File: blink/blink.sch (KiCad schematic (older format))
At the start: 2 parts

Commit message: Add 2nd LED
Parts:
- added D?: LED, symbol Device:LED
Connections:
- net +5V: now also D?.2 (A)
- net GND: now also D?.1 (K)
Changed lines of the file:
@@
 $EndComp
 Wire Wire Line
-	4750 2250 5300 2250
+	4750 2250 4850 2250
 $Comp
 L Device:R R1
@@
 $EndComp
 Wire Wire Line
-	5300 2850 4750 2850
+	5300 2850 4850 2850
 Wire Wire Line
 	4750 2850 4750 2950
@@
 	0    -1   -1   0
 $EndComp
+$Comp
+L Device:LED D?
+U 1 1 5FBDCB34
+P 4850 2550
+F 0 "D?" V 4889 2432 50  0000 R CNN
+F 1 "LED" V 4798 2432 50  0000 R CNN
+F 2 "" H 4850 2550 50  0001 C CNN
+F 3 "~" H 4850 2550 50  0001 C CNN
+	1    4850 2550
+	0    -1   -1   0
+$EndComp
+Wire Wire Line
+	4850 2400 4850 2250
+Connection ~ 4850 2250
+Wire Wire Line
+	4850 2250 5300 2250
+Wire Wire Line
+	4850 2700 4850 2850
+Connection ~ 4850 2850
+Wire Wire Line
+	4850 2850 4750 2850
 $EndSCHEMATC

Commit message: Added resistor
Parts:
- added R?: R, symbol Device:R
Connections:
- net GND: now also R?.2; no longer D?.1 (K)
- new net: D?.1 (K), R?.1
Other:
- moved on the sheet: D?
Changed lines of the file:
@@
 	1    0    0    -1
 $EndComp
-Wire Wire Line
-	4750 2250 4850 2250
 $Comp
 L Device:R R1
@@
 	1    0    0    -1
 $EndComp
-Wire Wire Line
-	5300 2850 4850 2850
 Wire Wire Line
 	4750 2850 4750 2950
@@
 L Device:LED D?
 U 1 1 5FBDCB34
-P 4850 2550
-F 0 "D?" V 4889 2432 50  0000 R CNN
-F 1 "LED" V 4798 2432 50  0000 R CNN
-F 2 "" H 4850 2550 50  0001 C CNN
-F 3 "~" H 4850 2550 50  0001 C CNN
-	1    4850 2550
+P 4850 2400
+F 0 "D?" V 4889 2282 50  0000 R CNN
+F 1 "LED" V 4798 2282 50  0000 R CNN
+F 2 "" H 4850 2400 50  0001 C CNN
+F 3 "~" H 4850 2400 50  0001 C CNN
+	1    4850 2400
 	0    -1   -1   0
 $EndComp
 Wire Wire Line
-	4850 2400 4850 2250
+	4750 2250 4850 2250
 Connection ~ 4850 2250
 Wire Wire Line
 	4850 2250 5300 2250
 Wire Wire Line
-	4850 2700 4850 2850
+	4750 2850 4850 2850
+$Comp
+L Device:R R?
+U 1 1 5FBDD47C
+P 4850 2700
+F 0 "R?" H 4920 2746 50  0000 L CNN
+F 1 "R" H 4920 2655 50  0000 L CNN
+F 2 "" V 4780 2700 50  0001 C CNN
+F 3 "~" H 4850 2700 50  0001 C CNN
+	1    4850 2700
+	1    0    0    -1
+$EndComp
 Connection ~ 4850 2850
 Wire Wire Line
-	4850 2850 4750 2850
+	4850 2850 5300 2850
 $EndSCHEMATC

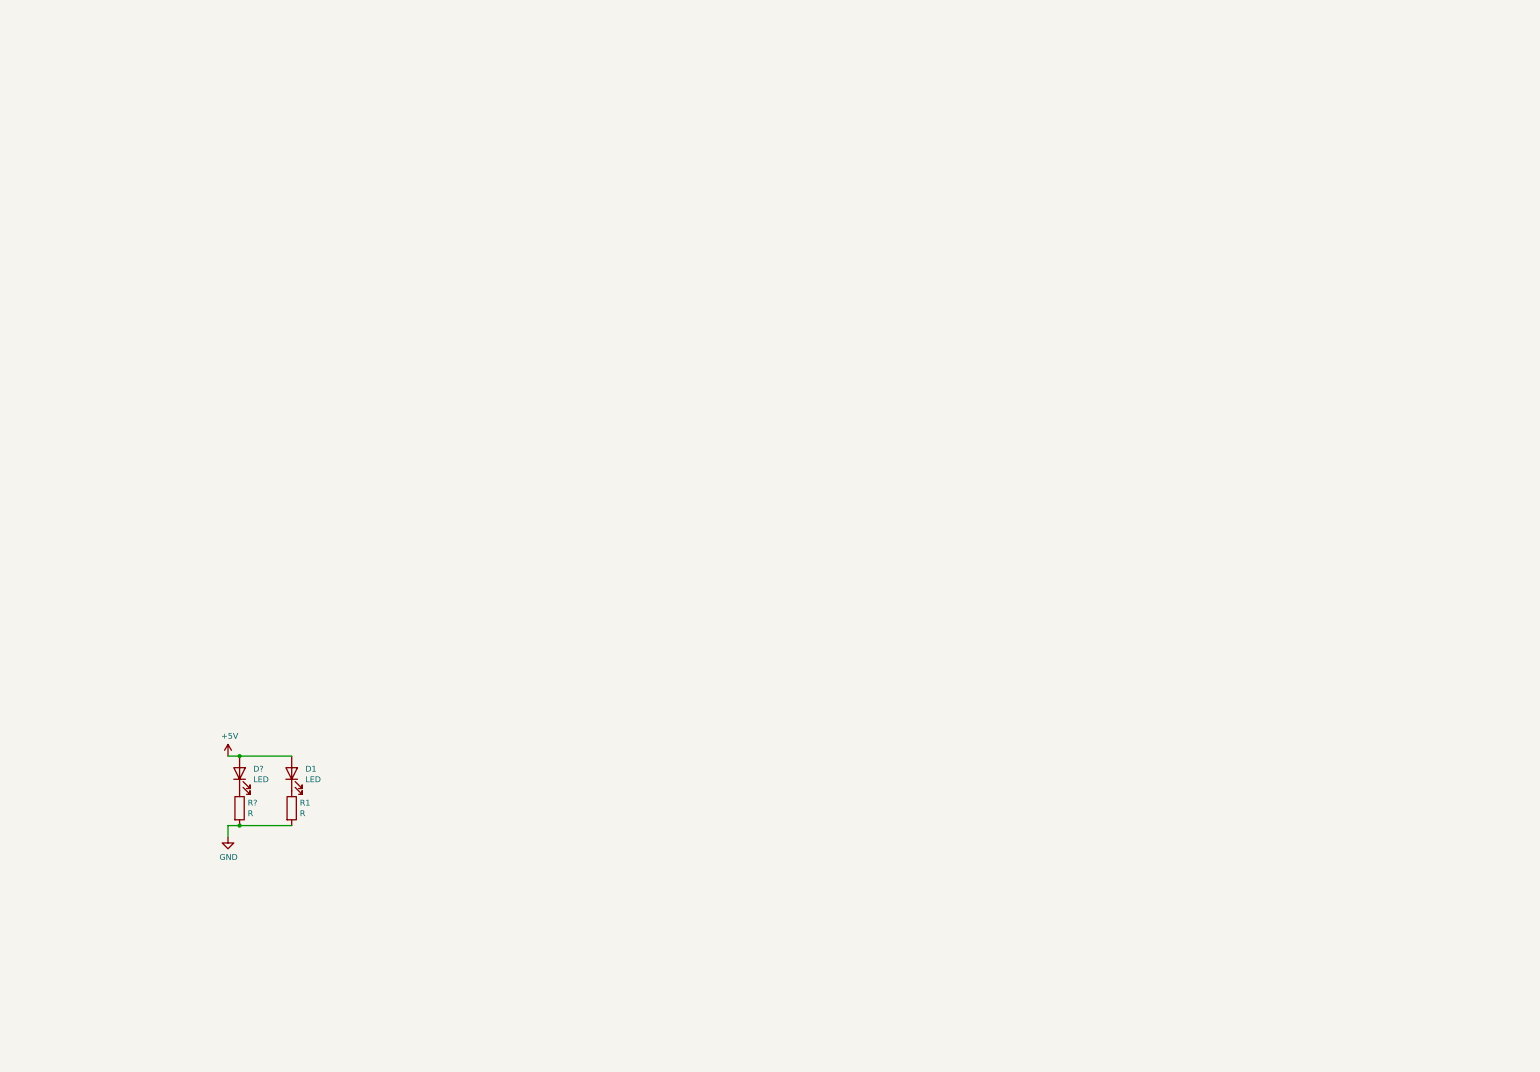
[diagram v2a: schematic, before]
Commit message: Added important battery
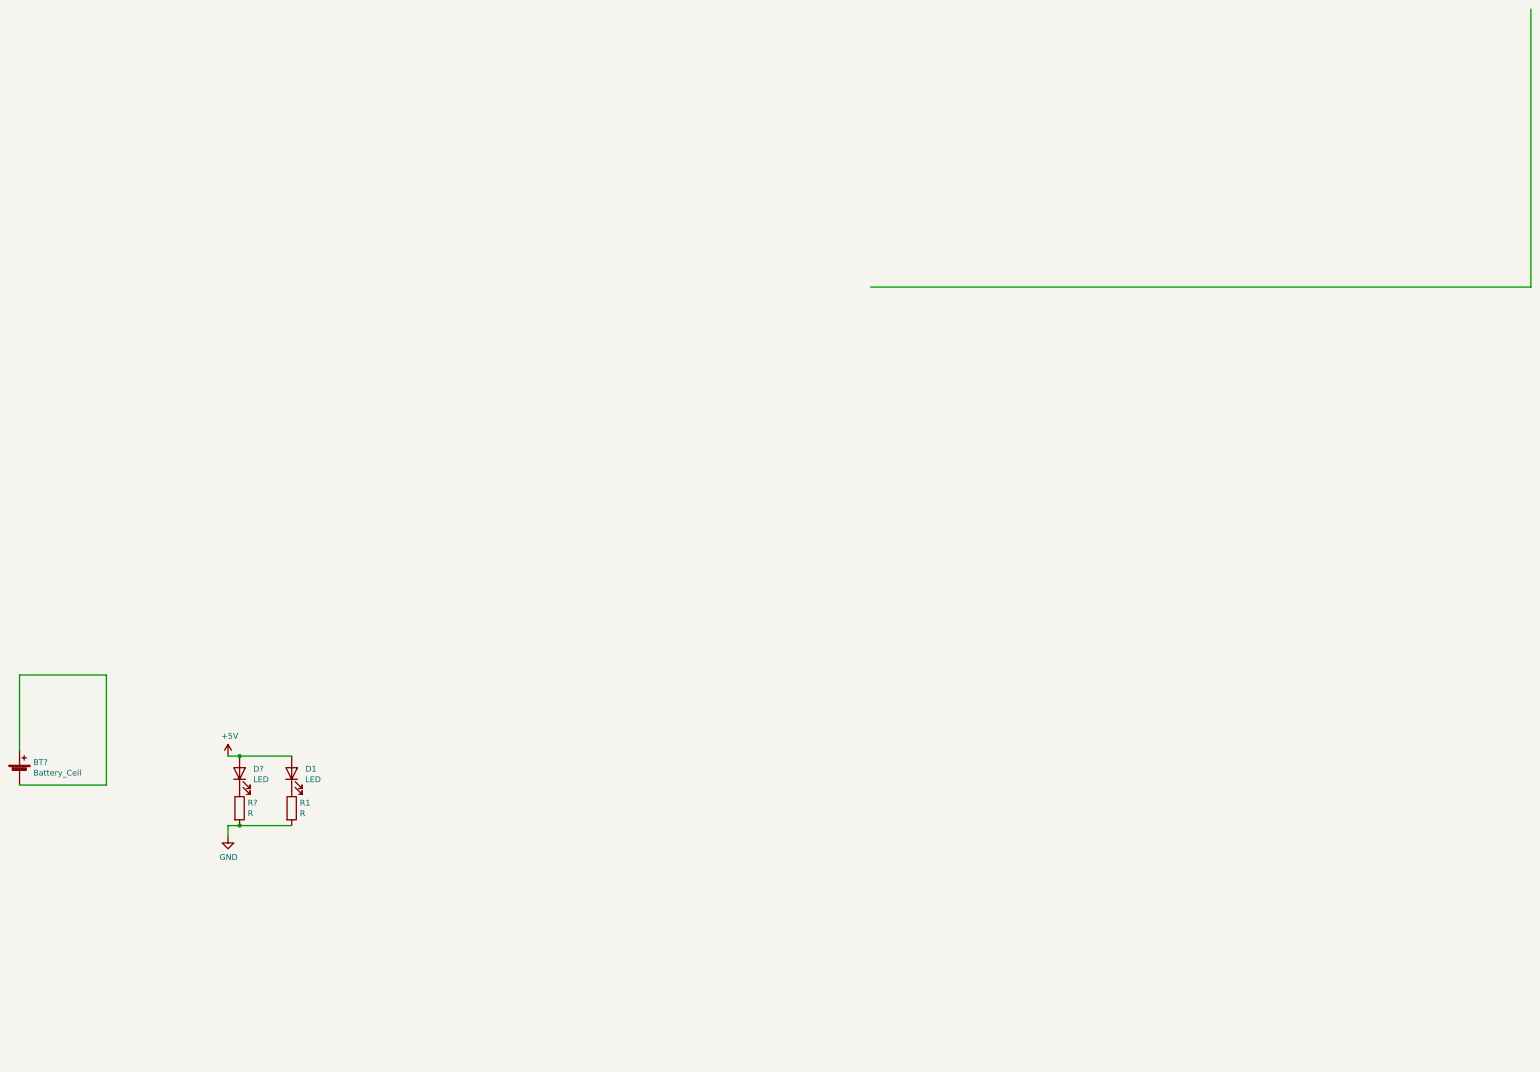
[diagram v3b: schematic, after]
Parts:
- added BT?: Battery_Cell, symbol Device:Battery_Cell
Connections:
- wire segments 5 -> 11
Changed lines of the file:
@@
 Wire Wire Line
 	4850 2850 5300 2850
+$Comp
+L Device:Battery_Cell BT?
+U 1 1 5FBDEFE5
+P 2950 2400
+F 0 "BT?" H 3068 2496 50  0000 L CNN
+F 1 "Battery_Cell" H 3068 2405 50  0000 L CNN
+F 2 "" V 2950 2460 50  0001 C CNN
+F 3 "~" V 2950 2460 50  0001 C CNN
+	1    2950 2400
+	1    0    0    -1
+$EndComp
+Wire Wire Line
+	10300 -1800 16000 -1800
+Wire Wire Line
+	16000 -1800 16000 -4200
+Wire Wire Line
+	2950 2200 2950 1550
+Wire Wire Line
+	2950 1550 3700 1550
+Wire Wire Line
+	3700 1550 3700 2500
+Wire Wire Line
+	3700 2500 2950 2500
 $EndSCHEMATC

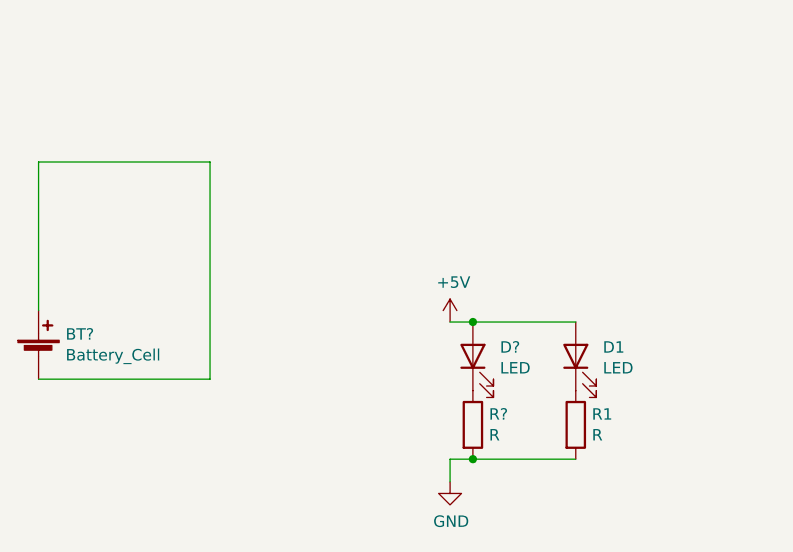
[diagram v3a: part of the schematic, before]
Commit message: Removed coin cell, added resistor values
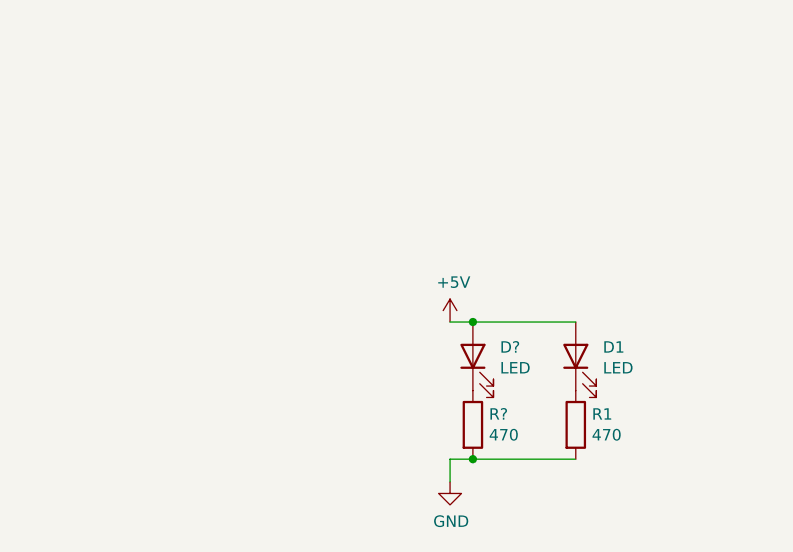
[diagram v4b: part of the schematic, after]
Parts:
- removed BT?: Battery_Cell, symbol Device:Battery_Cell
- R1, R?: value R -> 470
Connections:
- wire segments 11 -> 7
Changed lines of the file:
@@
 P 5300 2700
 F 0 "R1" H 5370 2746 50  0000 L CNN
-F 1 "R" H 5370 2655 50  0000 L CNN
+F 1 "470" H 5370 2655 50  0000 L CNN
 F 2 "Resistor_THT:R_Axial_DIN0204_L3.6mm_D1.6mm_P1.90mm_Vertical" V 5230 2700 50  0001 C CNN
 F 3 "~" H 5300 2700 50  0001 C CNN
@@
 P 4850 2700
 F 0 "R?" H 4920 2746 50  0000 L CNN
-F 1 "R" H 4920 2655 50  0000 L CNN
+F 1 "470" H 4920 2655 50  0000 L CNN
 F 2 "" V 4780 2700 50  0001 C CNN
 F 3 "~" H 4850 2700 50  0001 C CNN
@@
 Wire Wire Line
 	4850 2850 5300 2850
-$Comp
-L Device:Battery_Cell BT?
-U 1 1 5FBDEFE5
-P 2950 2400
-F 0 "BT?" H 3068 2496 50  0000 L CNN
-F 1 "Battery_Cell" H 3068 2405 50  0000 L CNN
-F 2 "" V 2950 2460 50  0001 C CNN
-F 3 "~" V 2950 2460 50  0001 C CNN
-	1    2950 2400
-	1    0    0    -1
-$EndComp
 Wire Wire Line
 	10300 -1800 16000 -1800
 Wire Wire Line
 	16000 -1800 16000 -4200
-Wire Wire Line
-	2950 2200 2950 1550
-Wire Wire Line
-	2950 1550 3700 1550
-Wire Wire Line
-	3700 1550 3700 2500
-Wire Wire Line
-	3700 2500 2950 2500
 $EndSCHEMATC

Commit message: Added a thingy
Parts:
- added BT?: Battery_Cell, symbol Device:Battery_Cell
- R1, R?: value 470 -> R
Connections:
- wire segments 7 -> 11
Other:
- moved on the sheet: R1, R?
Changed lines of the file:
@@
 L Device:R R1
 U 1 1 5FBDBA5D
-P 5300 2700
-F 0 "R1" H 5370 2746 50  0000 L CNN
-F 1 "470" H 5370 2655 50  0000 L CNN
-F 2 "Resistor_THT:R_Axial_DIN0204_L3.6mm_D1.6mm_P1.90mm_Vertical" V 5230 2700 50  0001 C CNN
-F 3 "~" H 5300 2700 50  0001 C CNN
-	1    5300 2700
+P 8050 4750
+F 0 "R1" H 8120 4796 50  0000 L CNN
+F 1 "R" H 8120 4705 50  0000 L CNN
+F 2 "Resistor_THT:R_Axial_DIN0204_L3.6mm_D1.6mm_P1.90mm_Vertical" V 7980 4750 50  0001 C CNN
+F 3 "~" H 8050 4750 50  0001 C CNN
+	1    8050 4750
 	1    0    0    -1
 $EndComp
 Wire Wire Line
-	4750 2850 4750 2950
+	7300 600  7300 700
 $Comp
 L power:GND #PWR0102
 U 1 1 5FBDBFDE
-P 4750 2950
-F 0 "#PWR0102" H 4750 2700 50  0001 C CNN
-F 1 "GND" H 4755 2777 50  0000 C CNN
-F 2 "" H 4750 2950 50  0001 C CNN
-F 3 "" H 4750 2950 50  0001 C CNN
-	1    4750 2950
+P 7300 700
+F 0 "#PWR0102" H 7300 450 50  0001 C CNN
+F 1 "GND" H 7305 527 50  0000 C CNN
+F 2 "" H 7300 700 50  0001 C CNN
+F 3 "" H 7300 700 50  0001 C CNN
+	1    7300 700
 	1    0    0    -1
 $EndComp
@@
 	4850 2250 5300 2250
 Wire Wire Line
-	4750 2850 4850 2850
+	7300 600  7400 600
 $Comp
 L Device:R R?
 U 1 1 5FBDD47C
-P 4850 2700
-F 0 "R?" H 4920 2746 50  0000 L CNN
-F 1 "470" H 4920 2655 50  0000 L CNN
-F 2 "" V 4780 2700 50  0001 C CNN
-F 3 "~" H 4850 2700 50  0001 C CNN
-	1    4850 2700
+P 7750 2200
+F 0 "R?" H 7820 2246 50  0000 L CNN
+F 1 "R" H 7820 2155 50  0000 L CNN
+F 2 "" V 7680 2200 50  0001 C CNN
+F 3 "~" H 7750 2200 50  0001 C CNN
+	1    7750 2200
 	1    0    0    -1
 $EndComp
-Connection ~ 4850 2850
 Wire Wire Line
-	4850 2850 5300 2850
+	7600 4900 8050 4900
+$Comp
+L Device:Battery_Cell BT?
+U 1 1 5FBDEFE5
+P 2950 2400
+F 0 "BT?" H 3068 2496 50  0000 L CNN
+F 1 "Battery_Cell" H 3068 2405 50  0000 L CNN
+F 2 "" V 2950 2460 50  0001 C CNN
+F 3 "~" V 2950 2460 50  0001 C CNN
+	1    2950 2400
+	1    0    0    -1
+$EndComp
 Wire Wire Line
 	10300 -1800 16000 -1800
 Wire Wire Line
 	16000 -1800 16000 -4200
+Wire Wire Line
+	2950 2200 2950 1550
+Wire Wire Line
+	2950 1550 3700 1550
+Wire Wire Line
+	3700 1550 3700 2500
+Wire Wire Line
+	3700 2500 2950 2500
 $EndSCHEMATC
